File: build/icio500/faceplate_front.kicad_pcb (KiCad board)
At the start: 4 copper layers, 38.1 x 133.3 mm, 3 parts

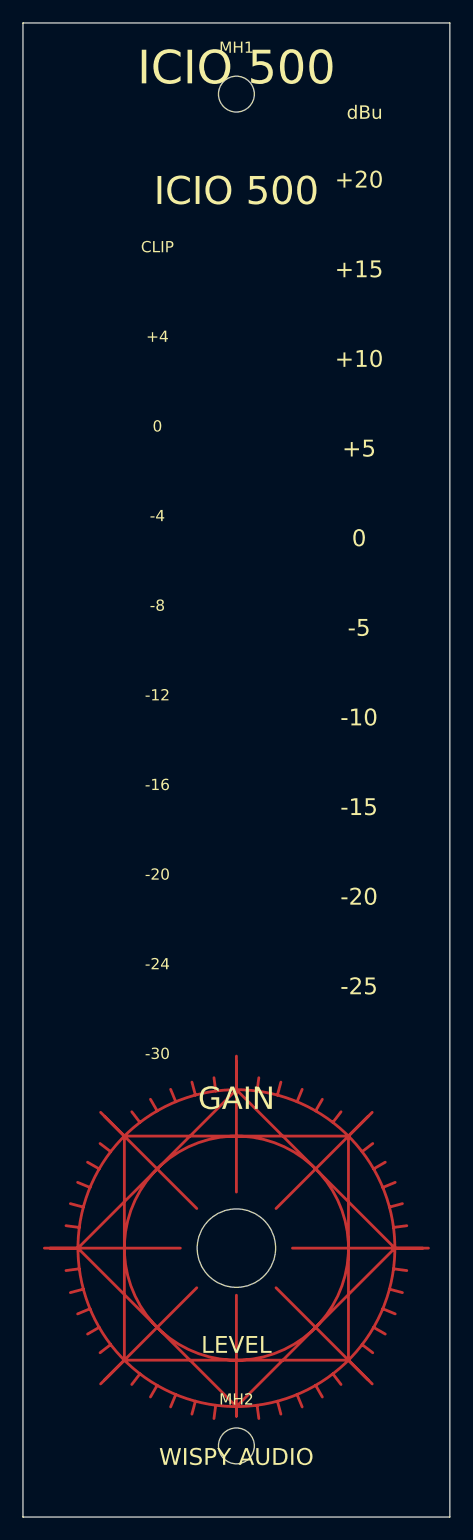
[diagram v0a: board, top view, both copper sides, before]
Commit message: Restore vertical Daisy Seed (U5 at 95,90), strip all words from faceplate leaving only right-side level indicators, center tongue with zero bottom bulk, and verify 0 DRC violations
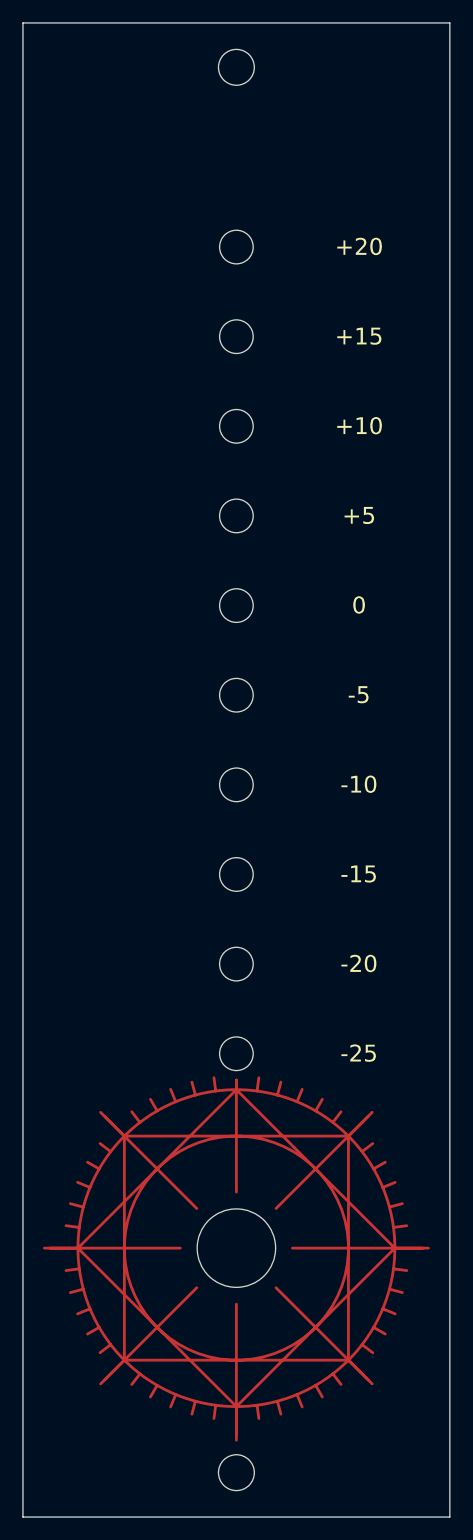
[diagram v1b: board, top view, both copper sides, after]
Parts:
- moved MH1 2.39 mm to (19.1, 3.96)
- moved MH2 2.39 mm to (19.1, 129.4)
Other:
- outline, holes or cut-outs redrawn
- board text removed: "+4"
- board text removed: "-12"
- board text removed: "-16"
- board text removed: "-24"
- board text removed: "-30"
- board text removed: "-4"
- board text removed: "-8"
- board text removed: "CLIP"
- board text removed: "GAIN"
- board text removed: "ICIO 500"
- board text removed: "LEVEL"
- board text removed: "WISPY AUDIO"
- board text removed: "dBu"

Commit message: Finalize VPR-500 mechanical mating, zero-DRC routing, unit 3D model scale, and JLCPCB packages
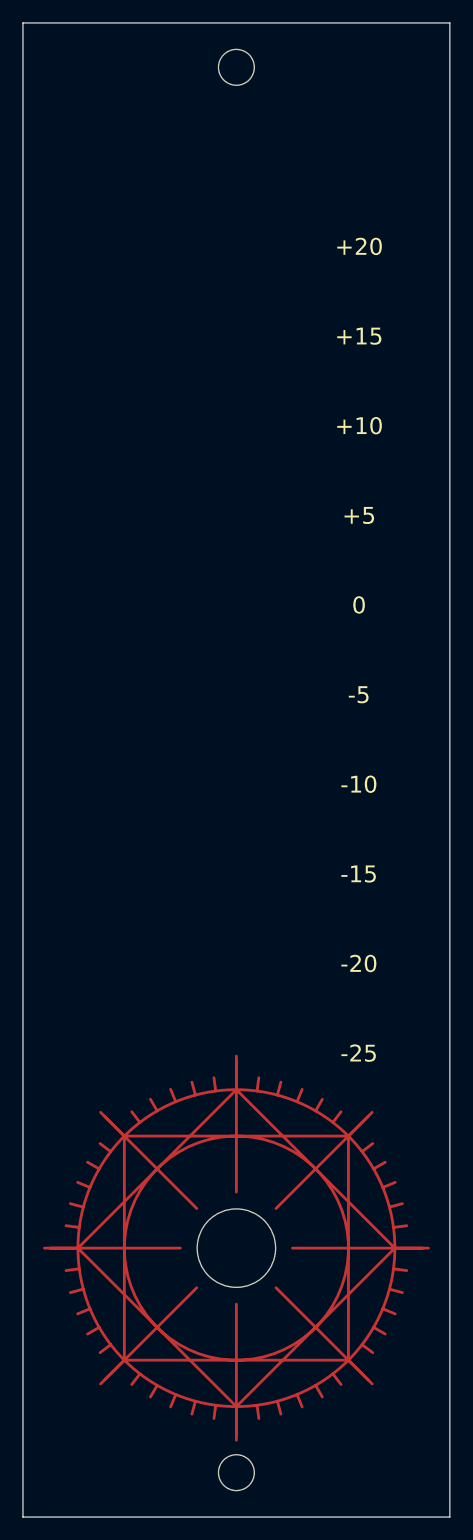
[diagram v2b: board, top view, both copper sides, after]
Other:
- outline, holes or cut-outs redrawn
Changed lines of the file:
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@@
 		(fp_line
 			(start 0 -14.1421)
-			(end 0 -15)
+			(end 0 -16.6421)
 			(stroke
 				(width 0.25)
@@
 		(fp_line
 			(start 0 -5)
-			(end 0 -15)
+			(end 0 -17.1421)
 			(stroke
 				(width 0.25)
@@
 		(fp_line
 			(start 0 -14.1421)
-			(end 0 -15)
+			(end 0 -16.6421)
 			(stroke
 				(width 0.25)
@@
 		(fp_line
 			(start 0 -5)
-			(end 0 -15)
+			(end 0 -17.1421)
 			(stroke
 				(width 0.25)
@@
 		(layer "Edge.Cuts")
 	)
-	(gr_circle
-		(center 19.05 20)
-		(end 20.55 20)
-		(stroke
-			(width 0.1)
-			(type default)
-		)
-		(fill no)
-		(layer "Edge.Cuts")
-	)
-	(gr_circle
-		(center 19.05 28)
-		(end 20.55 28)
-		(stroke
-			(width 0.1)
-			(type default)
-		)
-		(fill no)
-		(layer "Edge.Cuts")
-	)
-	(gr_circle
-		(center 19.05 36)
-		(end 20.55 36)
-		(stroke
-			(width 0.1)
-			(type default)
-		)
-		(fill no)
-		(layer "Edge.Cuts")
-	)
-	(gr_circle
-		(center 19.05 44)
-		(end 20.55 44)
-		(stroke
-			(width 0.1)
-			(type default)
-		)
-		(fill no)
-		(layer "Edge.Cuts")
-	)
-	(gr_circle
-		(center 19.05 52)
-		(end 20.55 52)
-		(stroke
-			(width 0.1)
-			(type default)
-		)
-		(fill no)
-		(layer "Edge.Cuts")
-	)
-	(gr_circle
-		(center 19.05 60)
-		(end 20.55 60)
-		(stroke
-			(width 0.1)
-			(type default)
-		)
-		(fill no)
-		(layer "Edge.Cuts")
-	)
-	(gr_circle
-		(center 19.05 68)
-		(end 20.55 68)
-		(stroke
-			(width 0.1)
-			(type default)
-		)
-		(fill no)
-		(layer "Edge.Cuts")
-	)
-	(gr_circle
-		(center 19.05 76)
-		(end 20.55 76)
-		(stroke
-			(width 0.1)
-			(type default)
-		)
-		(fill no)
-		(layer "Edge.Cuts")
-	)
-	(gr_circle
-		(center 19.05 84)
-		(end 20.55 84)
-		(stroke
-			(width 0.1)
-			(type default)
-		)
-		(fill no)
-		(layer "Edge.Cuts")
-	)
-	(gr_circle
-		(center 19.05 92)
-		(end 20.55 92)
-		(stroke
-			(width 0.1)
-			(type default)
-		)
-		(fill no)
-		(layer "Edge.Cuts")
-	)

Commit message: Restore authentic UI faceplate with complete VU meter, dial markings, and encoder hole; resolve carrier 5V trace and achieve 0 DRC violations across all boards
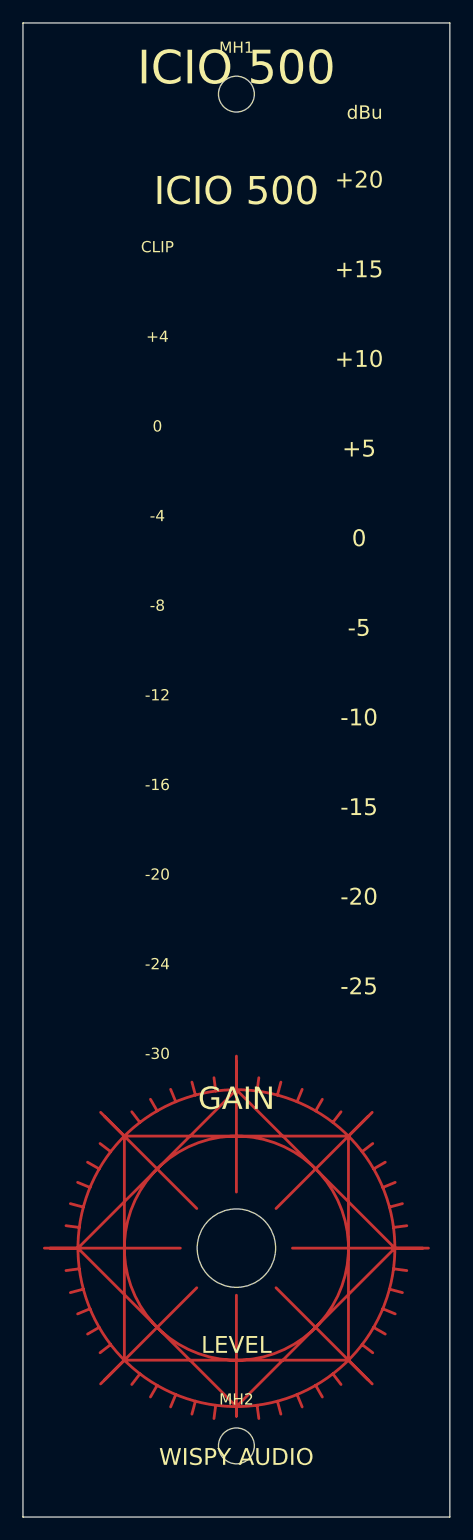
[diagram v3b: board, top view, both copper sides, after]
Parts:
- moved MH1 2.39 mm to (19.1, 6.35)
- moved MH2 2.39 mm to (19.1, 127.0)
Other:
- board text added: "+4"
- board text added: "-12"
- board text added: "-16"
- board text added: "-24"
- board text added: "-30"
- board text added: "-4"
- board text added: "-8"
- board text added: "CLIP"
- board text added: "GAIN"
- board text added: "ICIO 500"
- board text added: "LEVEL"
- board text added: "WISPY AUDIO"
- board text added: "dBu"
